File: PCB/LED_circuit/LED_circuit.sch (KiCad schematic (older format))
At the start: 14 parts

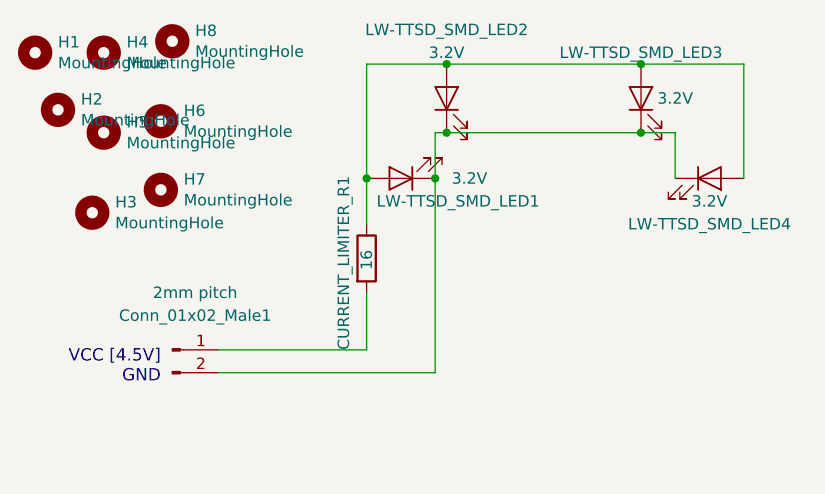
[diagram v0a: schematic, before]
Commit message: Added LEDs to have the option of installing more if needed, fixed ground layer on main board to be connected everywhere, rewired pins to ease soldering
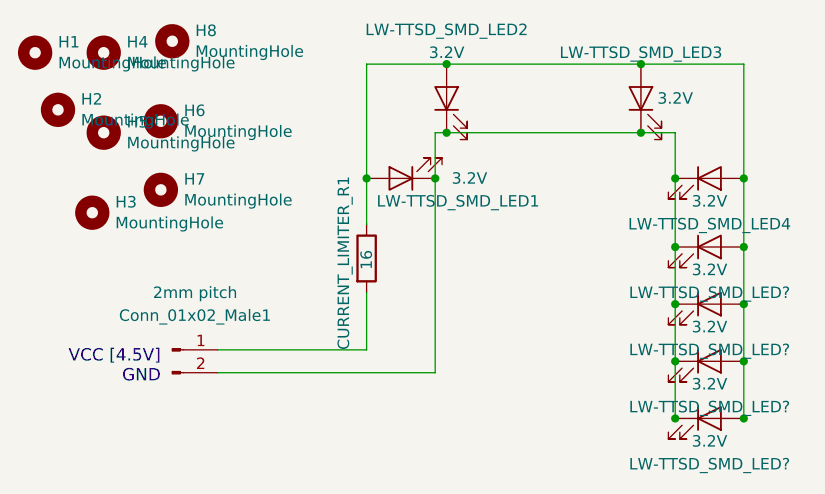
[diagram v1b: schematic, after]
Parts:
- added LW-TTSD_SMD_LED? (x4): 3.2V, LED_SMD:LED_PLCC-2, symbol Device:LED
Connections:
- net at Conn_01x02_Male1.2 (Pin_2), LW-TTSD_SMD_LED1.1 (K), LW-TTSD_SMD_LED2.1 (K)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: now also LW-TTSD_SMD_LED?.1 (K), LW-TTSD_SMD_LED?.1 (K), LW-TTSD_SMD_LED?.1 (K), LW-TTSD_SMD_LED?.1 (K)
- net at CURRENT_LIMITER_R1.1, LW-TTSD_SMD_LED1.2 (A), LW-TTSD_SMD_LED2.2 (A)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: now also LW-TTSD_SMD_LED?.2 (A), LW-TTSD_SMD_LED?.2 (A), LW-TTSD_SMD_LED?.2 (A), LW-TTSD_SMD_LED?.2 (A)
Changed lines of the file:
@@
 	1    0    0    -1
 $EndComp
+$Comp
+L Device:LED LW-TTSD_SMD_LED?
+U 1 1 5CA375C0
+P 6900 4250
+F 0 "LW-TTSD_SMD_LED?" H 6900 4050 50  0000 C CNN
+F 1 "3.2V" H 6900 4150 50  0000 C CNN
+F 2 "LED_SMD:LED_PLCC-2" H 6900 4250 50  0001 C CNN
+F 3 "~" H 6900 4250 50  0001 C CNN
+	1    6900 4250
+	1    0    0    -1
+$EndComp
+$Comp
+L Device:LED LW-TTSD_SMD_LED?
+U 1 1 5CA375F6
+P 6900 4500
+F 0 "LW-TTSD_SMD_LED?" H 6900 4300 50  0000 C CNN
+F 1 "3.2V" H 6900 4400 50  0000 C CNN
+F 2 "LED_SMD:LED_PLCC-2" H 6900 4500 50  0001 C CNN
+F 3 "~" H 6900 4500 50  0001 C CNN
+	1    6900 4500
+	1    0    0    -1
+$EndComp
+$Comp
+L Device:LED LW-TTSD_SMD_LED?
+U 1 1 5CA3762C
+P 6900 4750
+F 0 "LW-TTSD_SMD_LED?" H 6900 4550 50  0000 C CNN
+F 1 "3.2V" H 6900 4650 50  0000 C CNN
+F 2 "LED_SMD:LED_PLCC-2" H 6900 4750 50  0001 C CNN
+F 3 "~" H 6900 4750 50  0001 C CNN
+	1    6900 4750
+	1    0    0    -1
+$EndComp
+$Comp
+L Device:LED LW-TTSD_SMD_LED?
+U 1 1 5CA37664
+P 6900 5000
+F 0 "LW-TTSD_SMD_LED?" H 6900 4800 50  0000 C CNN
+F 1 "3.2V" H 6900 4900 50  0000 C CNN
+F 2 "LED_SMD:LED_PLCC-2" H 6900 5000 50  0001 C CNN
+F 3 "~" H 6900 5000 50  0001 C CNN
+	1    6900 5000
+	1    0    0    -1
+$EndComp
+Wire Wire Line
+	7050 3950 7050 4250
+Connection ~ 7050 3950
+Wire Wire Line
+	7050 4250 7050 4500
+Connection ~ 7050 4250
+Wire Wire Line
+	7050 4500 7050 4750
+Connection ~ 7050 4500
+Wire Wire Line
+	7050 4750 7050 5000
+Connection ~ 7050 4750
+Wire Wire Line
+	6750 5000 6750 4750
+Wire Wire Line
+	6750 4750 6750 4500
+Connection ~ 6750 4750
+Wire Wire Line
+	6750 4500 6750 4250
+Connection ~ 6750 4500
+Wire Wire Line
+	6750 3950 6750 4250
+Connection ~ 6750 3950
+Connection ~ 6750 4250
+Connection ~ 7050 5000
+Connection ~ 6750 5000
 $EndSCHEMATC
